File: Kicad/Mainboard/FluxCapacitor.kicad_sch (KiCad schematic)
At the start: 90 parts, among them J1 PJ-002A, J2 TM_1, J3 TM_2, J7 TM_4, J8 TM_2, J9 RELAY, M1 SYS_FAN, Q2 IRF4905PBF, Q3 2N7000, Q4 2N7000, U1 OKI-78SR-5_1.5-W36-C, U2 ESP32_DEVBOARD

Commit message: Continued mainboard layout
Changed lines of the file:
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@@
 	)
 	(rectangle
-		(start 15.24 67.31)
-		(end 80.01 194.31)
-		(stroke
-			(width 0)
-			(type default)
-		)
-		(fill
-			(type none)
-		)
-	)
-	(rectangle
 		(start 105.664 107.95)
 		(end 173.99 194.31)
@@
 		(dnp no)
 		(property "Reference" "D1"
-			(at 25.4 48.26 0)
+			(at 29.21 48.768 0)
 			(show_name no)
 			(do_not_autoplace no)

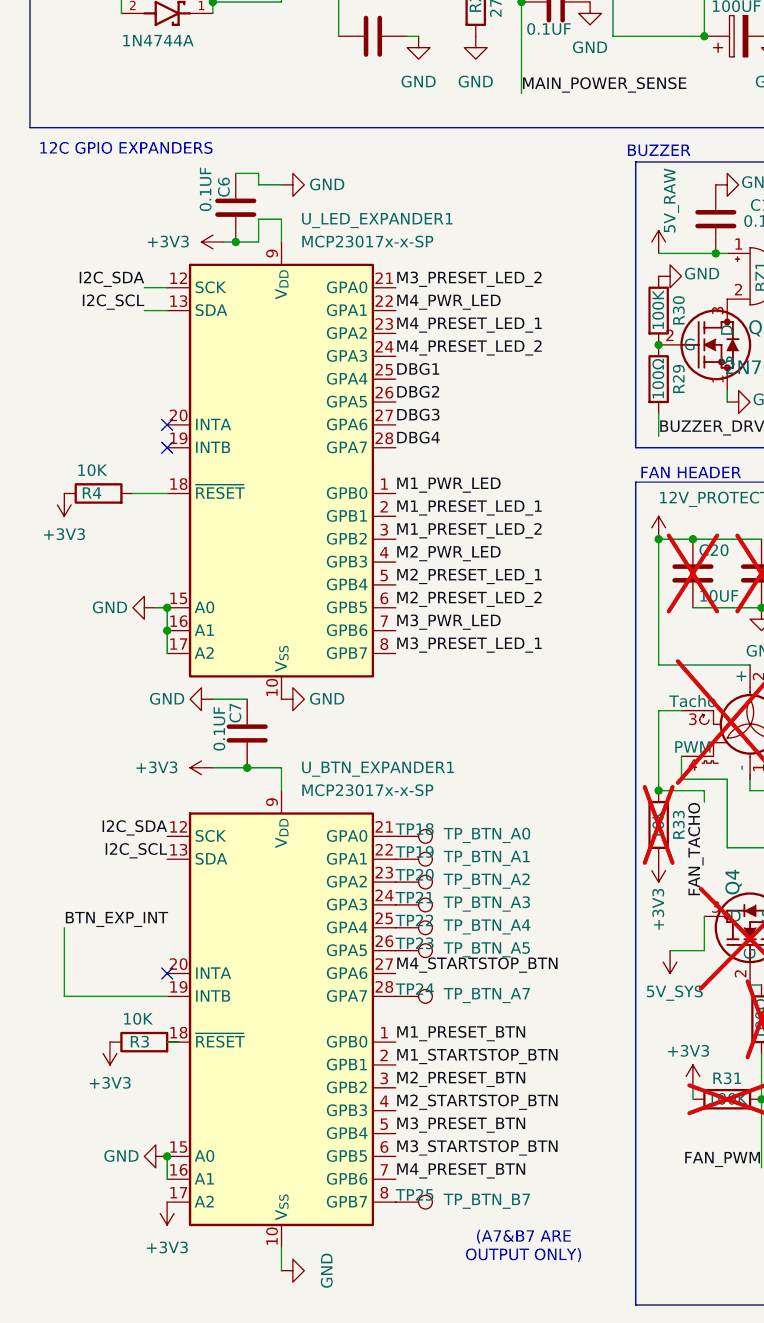
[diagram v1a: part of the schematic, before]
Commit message: Finished Mainboard Layout
-Now all that needs to be done is to resolve all DRC errors
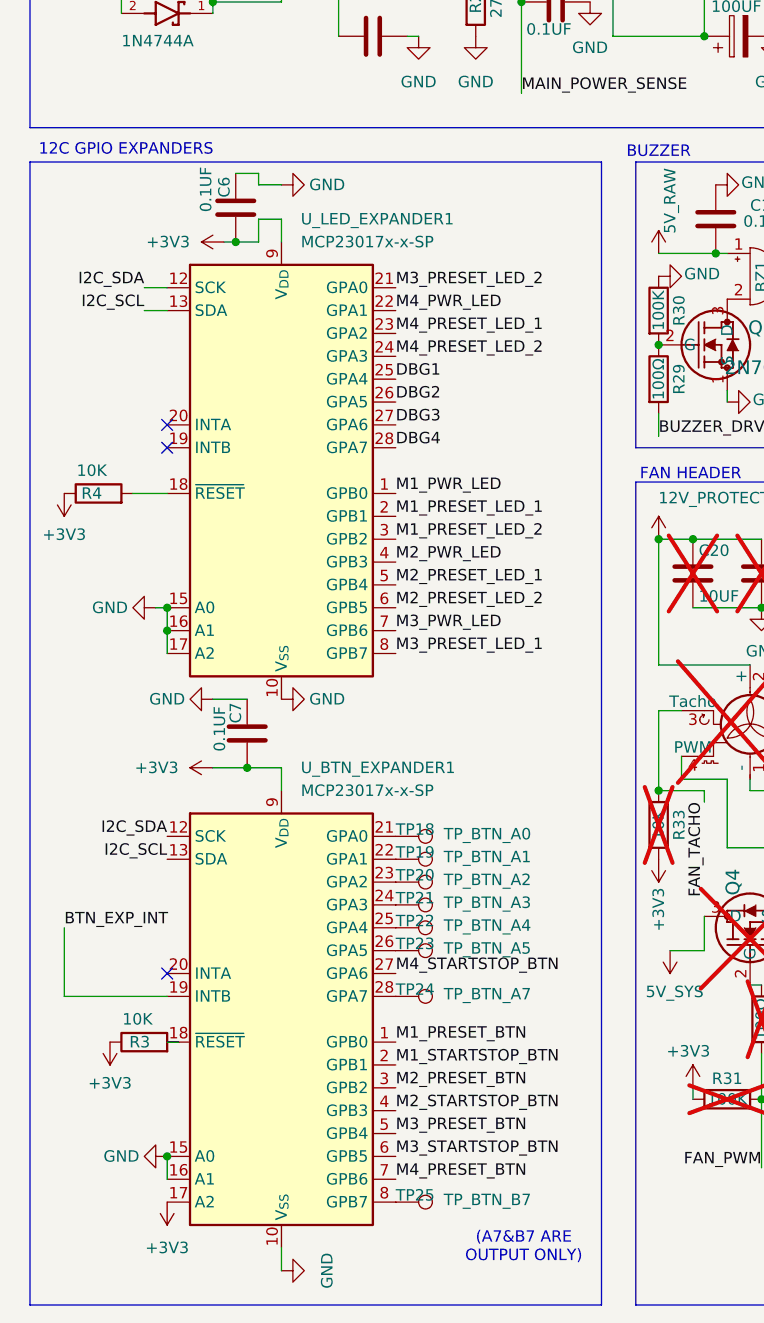
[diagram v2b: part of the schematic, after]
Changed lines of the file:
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@@
+	)
+	(rectangle
+		(start 15.24 67.31)
+		(end 78.74 194.31)
+		(stroke
+			(width 0)
+			(type default)
+		)
+		(fill
+			(type none)
+		)
 	)
 	(rectangle

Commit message: Made relay splitter daughterboard
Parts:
- TP15, TP16, TP17, TP18, TP19, TP20, TP21, TP22, TP23, TP24, TP25, TP6, TP7: footprint FluxCapacitor:TestPoint_Pad_D2.0mm -> FluxCapacitor:TestPoint_Pad_D1.5mm
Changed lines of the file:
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@@
 			)
 		)
-		(property "Footprint" "FluxCapacitor:TestPoint_Pad_D2.0mm"
+		(property "Footprint" "FluxCapacitor:TestPoint_Pad_D1.5mm"
 			(at 55.88 147.32 0)
 			(hide yes)
@@
 			)
 		)
-		(property "Footprint" "FluxCapacitor:TestPoint_Pad_D2.0mm"
+		(property "Footprint" "FluxCapacitor:TestPoint_Pad_D1.5mm"
 			(at 151.13 39.37 0)
 			(hide yes)
@@
 			)
 		)
-		(property "Footprint" "FluxCapacitor:TestPoint_Pad_D2.0mm"
+		(property "Footprint" "FluxCapacitor:TestPoint_Pad_D1.5mm"
 			(at 55.88 187.96 0)
 			(hide yes)
@@
 			)
 		)
-		(property "Footprint" "FluxCapacitor:TestPoint_Pad_D2.0mm"
+		(property "Footprint" "FluxCapacitor:TestPoint_Pad_D1.5mm"
 			(at 151.13 49.53 0)
 			(hide yes)
@@
 			)
 		)
-		(property "Footprint" "FluxCapacitor:TestPoint_Pad_D2.0mm"
+		(property "Footprint" "FluxCapacitor:TestPoint_Pad_D1.5mm"
 			(at 55.88 165.1 0)
 			(hide yes)
@@
 			)
 		)
-		(property "Footprint" "FluxCapacitor:TestPoint_Pad_D2.0mm"
+		(property "Footprint" "FluxCapacitor:TestPoint_Pad_D1.5mm"
 			(at 151.13 46.99 0)
 			(hide yes)
@@
 			)
 		)
-		(property "Footprint" "FluxCapacitor:TestPoint_Pad_D2.0mm"
+		(property "Footprint" "FluxCapacitor:TestPoint_Pad_D1.5mm"
 			(at 55.88 152.4 0)
 			(hide yes)
@@
 			)
 		)
-		(property "Footprint" "FluxCapacitor:TestPoint_Pad_D2.0mm"
+		(property "Footprint" "FluxCapacitor:TestPoint_Pad_D1.5mm"
 			(at 55.88 154.94 0)
 			(hide yes)
@@
 			)
 		)
-		(property "Footprint" "FluxCapacitor:TestPoint_Pad_D2.0mm"
+		(property "Footprint" "FluxCapacitor:TestPoint_Pad_D1.5mm"
 			(at 55.88 157.48 0)
 			(hide yes)
@@
 			)
 		)
-		(property "Footprint" "FluxCapacitor:TestPoint_Pad_D2.0mm"
+		(property "Footprint" "FluxCapacitor:TestPoint_Pad_D1.5mm"
 			(at 55.88 160.02 0)
 			(hide yes)
@@
 			)
 		)
-		(property "Footprint" "FluxCapacitor:TestPoint_Pad_D2.0mm"
+		(property "Footprint" "FluxCapacitor:TestPoint_Pad_D1.5mm"
 			(at 151.13 34.29 0)
 			(hide yes)
@@
 			)
 		)
-		(property "Footprint" "FluxCapacitor:TestPoint_Pad_D2.0mm"
+		(property "Footprint" "FluxCapacitor:TestPoint_Pad_D1.5mm"
 			(at 151.13 41.91 0)
 			(hide yes)
@@
 			)
 		)
-		(property "Footprint" "FluxCapacitor:TestPoint_Pad_D2.0mm"
+		(property "Footprint" "FluxCapacitor:TestPoint_Pad_D1.5mm"
 			(at 55.88 149.86 0)
 			(hide yes)
